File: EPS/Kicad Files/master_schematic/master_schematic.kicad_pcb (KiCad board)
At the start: 2 copper layers, 96 x 90 mm, 79 parts, among them J1 USB_C_Receptacle, J2 436500212, J3 Conn_02x20_Odd_Even, J4 Conn_01x05_Female, Q1 FZT688BTA, Q2 FZT688BTA, U1 RPM5.0-2.0, U2 RPM5.0-2.0, U3 RPM3.3-2.0, U4 INA3221, U5 MAX77757JEFG435+, U6 MAX17055EWL+T, U7 ATA6560-GAQW-VAO, U8 PIC18F27Q84-E/SP

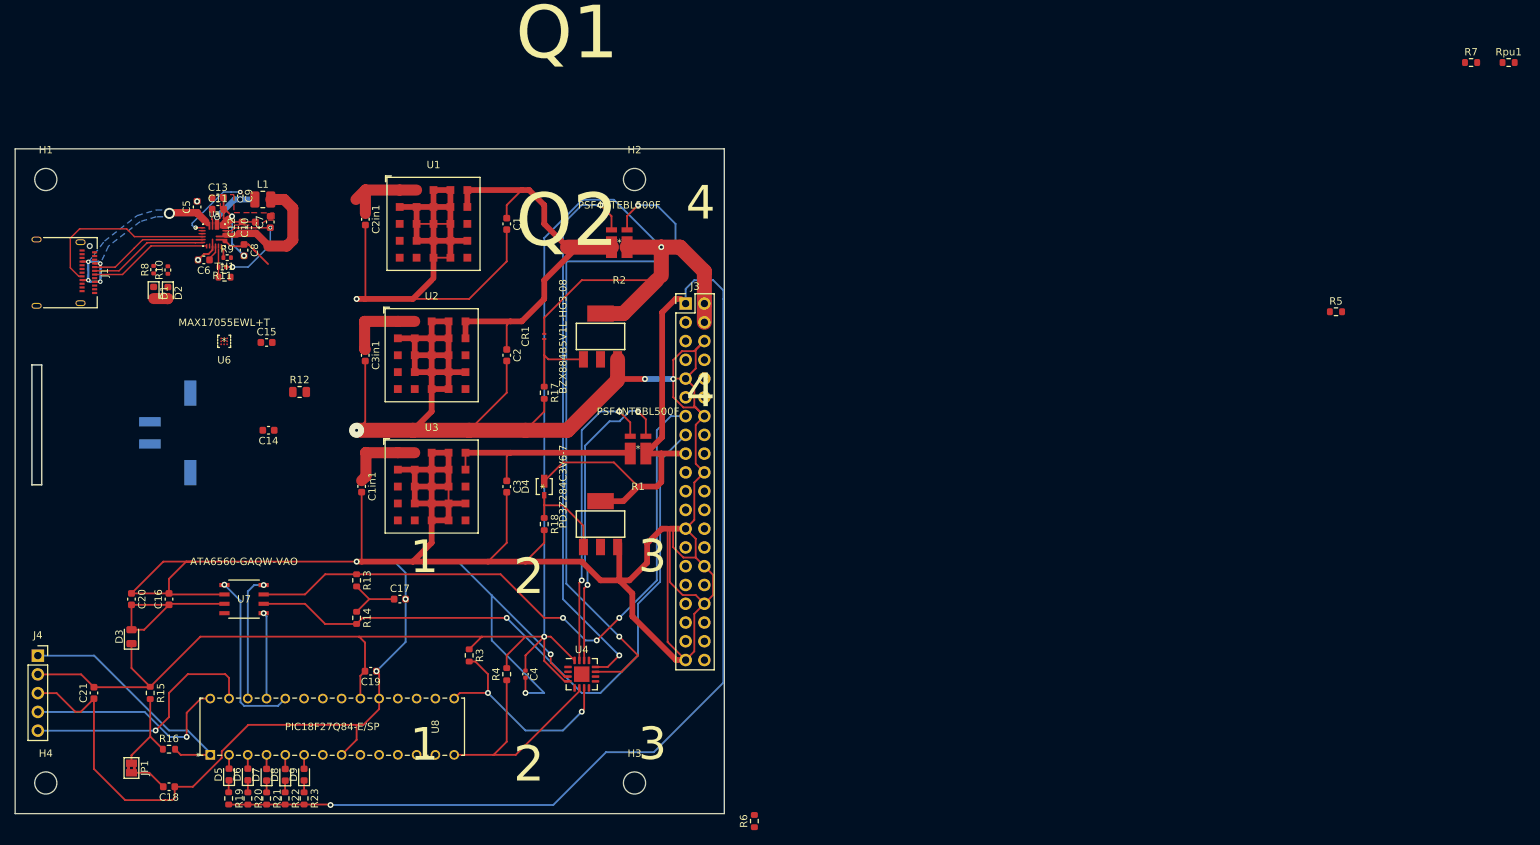
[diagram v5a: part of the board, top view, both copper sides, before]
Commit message: all traces routed (EPS)
all nets, traces, etc connected.....now we need to run DRC...errors are inevitable
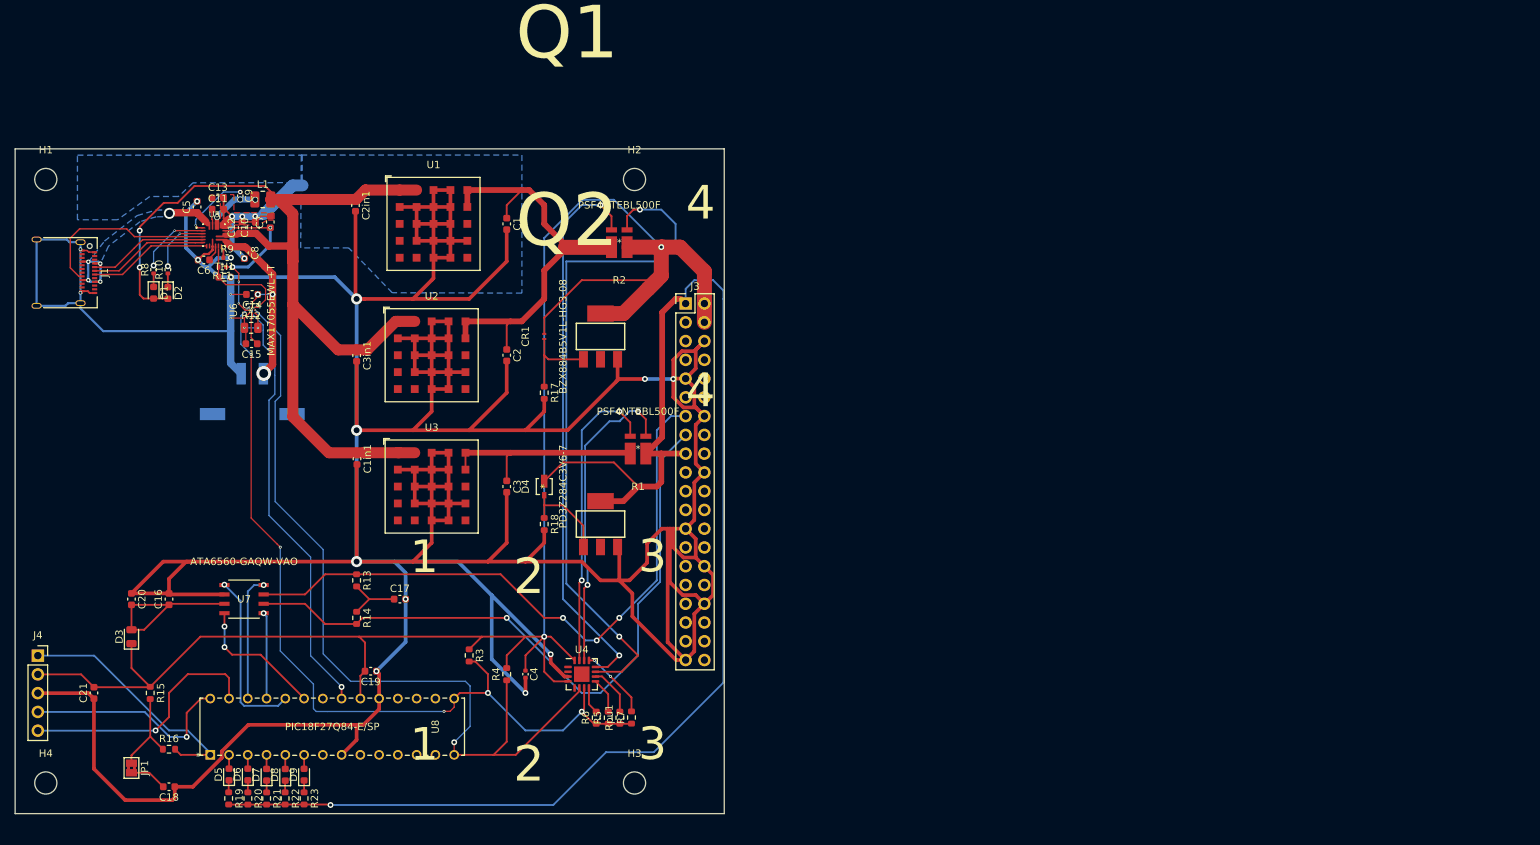
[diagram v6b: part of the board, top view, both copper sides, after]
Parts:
- moved Rpu1 149.5 mm to (119.5, 132.9), turned to 90 degrees
- moved R7 144.2 mm to (121.0, 132.9), turned to 90 degrees
- moved R5 112.8 mm to (117.9, 132.9), turned to 90 degrees
- moved R6 25.6 mm to (116.3, 132.9)
- moved C14 18.5 mm to (69.7, 75.6)
- moved R12 10.9 mm to (69.5, 80.1)
- moved J2 9.20 mm to (69.7, 91.4), turned to 180 degrees
- moved U6 5.68 mm to (69.7, 77.7), turned to -90 degrees
- moved C1in1 3.79 mm to (83.9, 97.8)
- moved C2in1 2.30 mm to (83.7, 63.6)
- moved C15 2.04 mm to (69.6, 82.3), turned to 180 degrees
- moved C3in1 1.17 mm to (83.8, 83.9)
- moved C8 0.37 mm to (68.6, 70.0)
- moved R10 0.05 mm to (58.3, 72.2)
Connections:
- J2 pad P1: /charge schem/V_BAT -> unconnected-(J2-PadP1)
- J2 pad P2: /charge schem/V_BAT -> unconnected-(J2-PadP2)
- U6 pad B2: /ALRT -> ALRT
- U8 pad 10: /ColoradoCUBE_Payload/X -> unconnected-(U8-Pad10)
- U8 pad 11: /ColoradoCUBE_Payload/X -> unconnected-(U8-Pad11)
- U8 pad 12: /ColoradoCUBE_Payload/X -> unconnected-(U8-Pad12)
- U8 pad 13: /ColoradoCUBE_Payload/X -> unconnected-(U8-Pad13)
- U8 pad 16: /ColoradoCUBE_Payload/X -> unconnected-(U8-Pad16)
- U8 pad 17: /ColoradoCUBE_Payload/X -> unconnected-(U8-Pad17)
- U8 pad 18: /ColoradoCUBE_Payload/X -> unconnected-(U8-Pad18)
- U8 pad 21: /ColoradoCUBE_Payload/ALRT -> ALRT
- U8 pad 9: /ColoradoCUBE_Payload/X -> unconnected-(U8-Pad9)
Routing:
- net /ColoradoCUBE_Payload/5V: track 304.4 -> 477.6 mm, vias 4 -> 10
- net GND: track 675.1 -> 830.7 mm, vias 11 -> 19
- net /charge schem/SYSPOWER: track 53.3 -> 137.0 mm, vias 0 -> 2
- net ALRT: track 0.00 -> 58.3 mm, vias 0 -> 2
- net /charge schem/V_BAT: track 6.96 -> 25.9 mm, vias 0 -> 3
- net /ColoradoCUBE_Payload/CAN_Transceiver/CAN_RX: track 0.00 -> 18.2 mm, vias 0 -> 2
- net GNDPWR: track 15.6 -> 29.6 mm, vias 2 -> 4
- net Net-(R11-Pad2): track 4.14 -> 14.5 mm
- net /converterschematic/TC: track 0.00 -> 10.1 mm, vias 0 -> 2
- net Net-(R8-Pad2): track 0.56 -> 9.76 mm, vias 0 -> 2
- net Net-(R10-Pad2): track 0.56 -> 8.24 mm, vias 0 -> 2
- net Net-(C7-Pad1): track 15.9 -> 23.1 mm, vias 2 -> 4
- net /converterschematic/PV: track 0.00 -> 6.65 mm
- net /converterschematic/CRT: track 0.00 -> 4.80 mm
- net Net-(C15-Pad1): track 0.00 -> 4.49 mm
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- added copper zone on B.Cu, net GNDPWR
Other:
- outline, holes or cut-outs redrawn

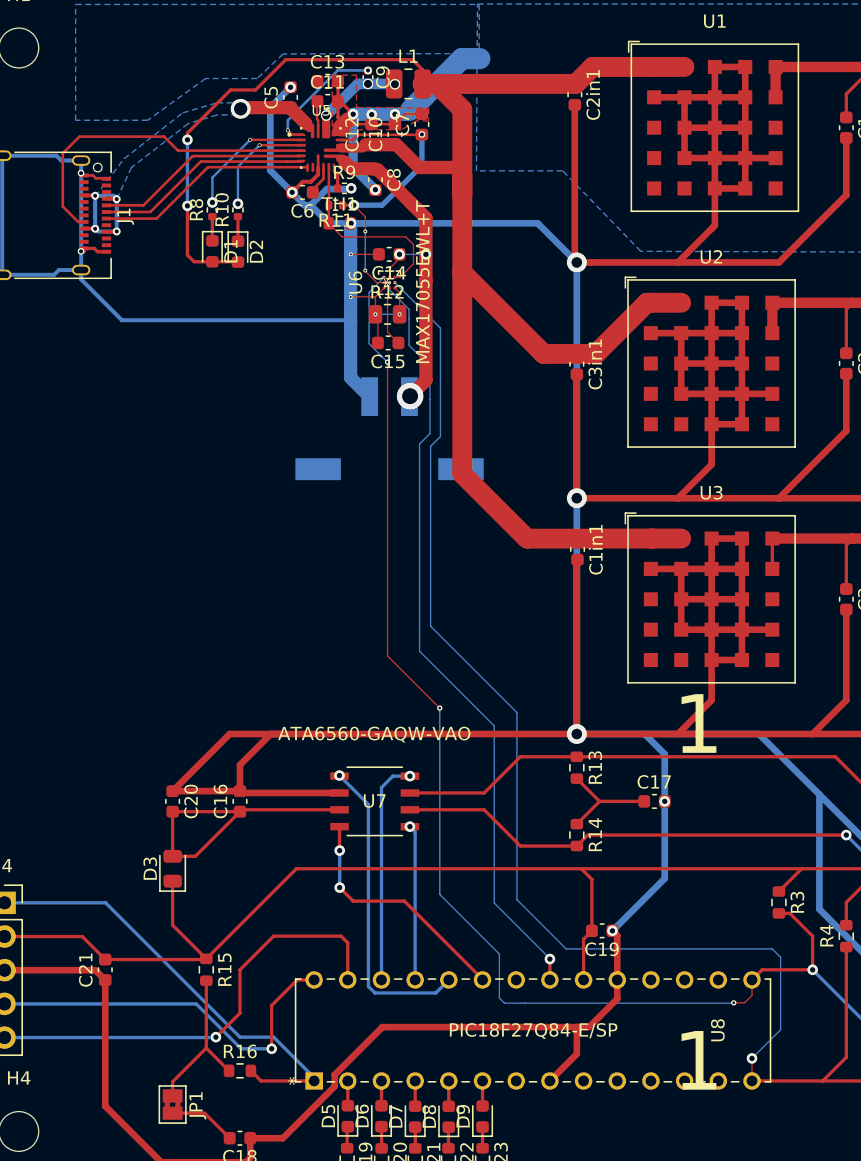
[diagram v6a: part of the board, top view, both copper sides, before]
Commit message: [EPS] updated *some* DRC rules...
there are a lot
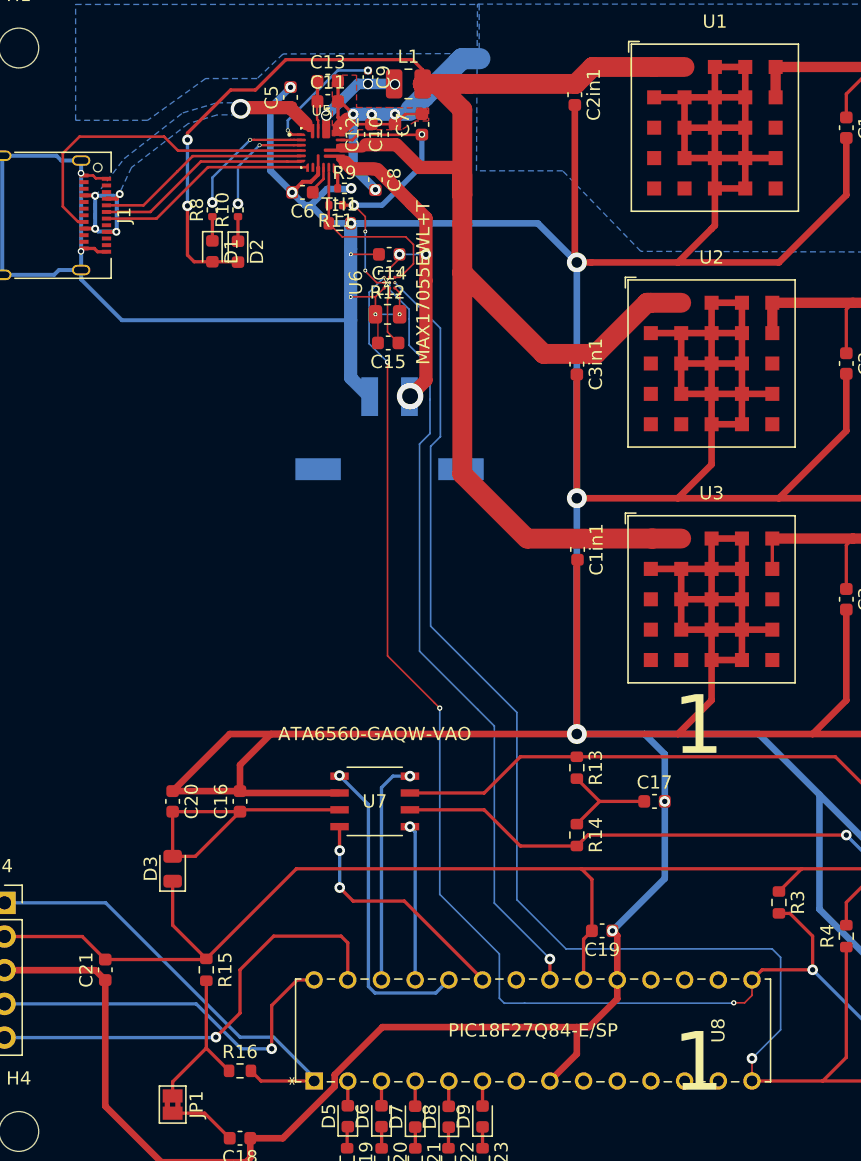
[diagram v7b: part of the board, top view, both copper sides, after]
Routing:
- net Net-(C11-Pad1): track 1.57 -> 3.10 mm
- net Net-(C5-Pad1): track 17.1 -> 17.9 mm

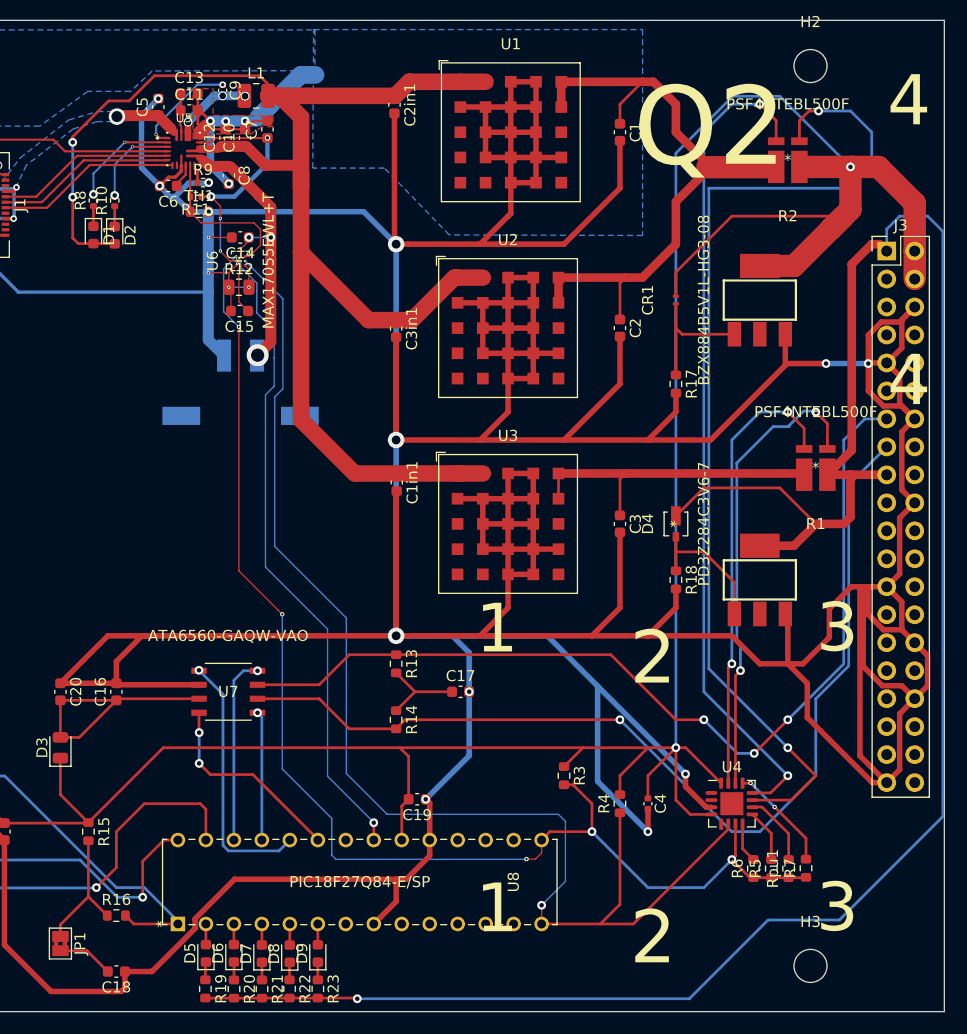
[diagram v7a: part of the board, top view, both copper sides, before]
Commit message: [EPS] updated DRC errors
fixed/updated rules to have no errors. however the dimensions might not work with manufacturers.... also, silkscreens need to be moved/resized
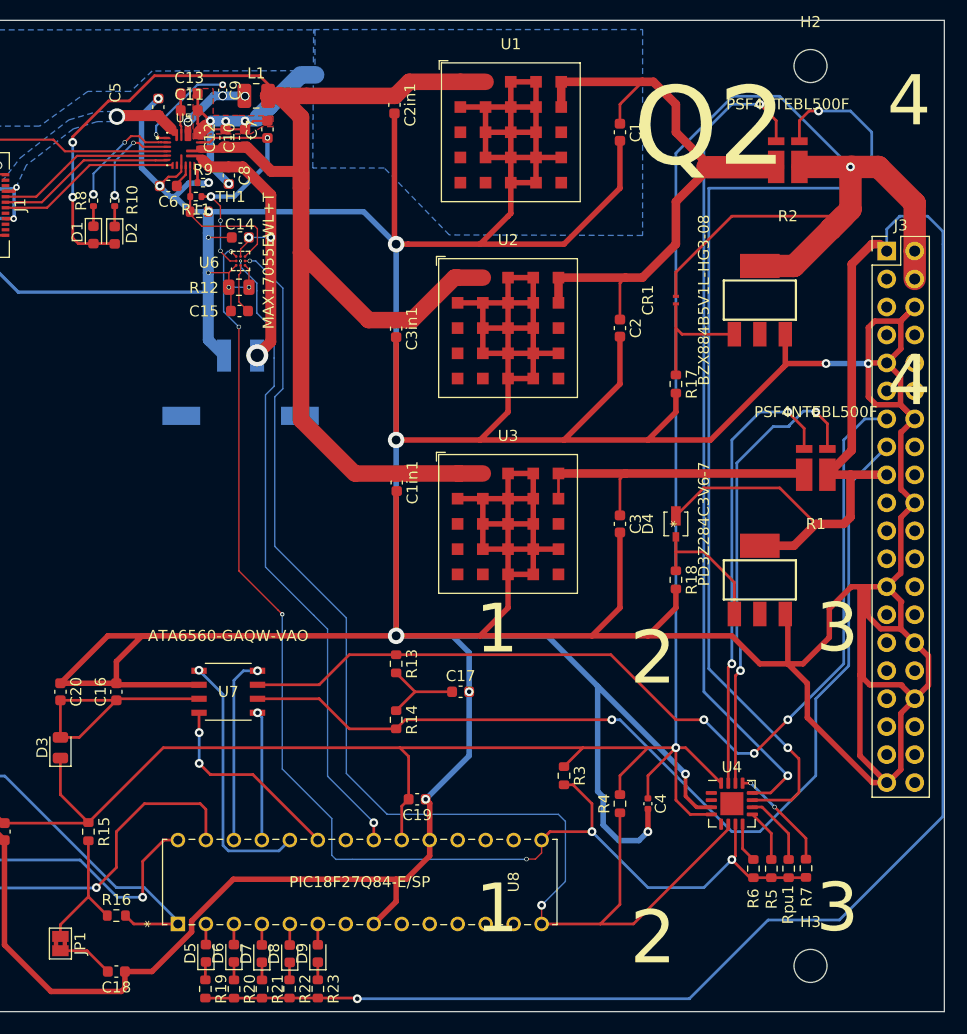
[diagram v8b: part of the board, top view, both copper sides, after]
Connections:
- J2 pad 2: unconnected-(J2-Pad2) -> /charge schem/V_BAT
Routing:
- net GND: track 830.3 -> 834.1 mm
- net /ColoradoCUBE_Payload/5V: track 477.6 -> 479.1 mm
- net Net-(R2-Pad3): track 92.0 -> 90.7 mm
- net /charge schem/V_BAT: track 25.9 -> 26.6 mm
